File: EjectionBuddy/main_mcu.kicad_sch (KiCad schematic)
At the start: 8 parts, among them SW2 SW_Push, SW3 SW_Push, U11 ESP32-S3-MINI-1

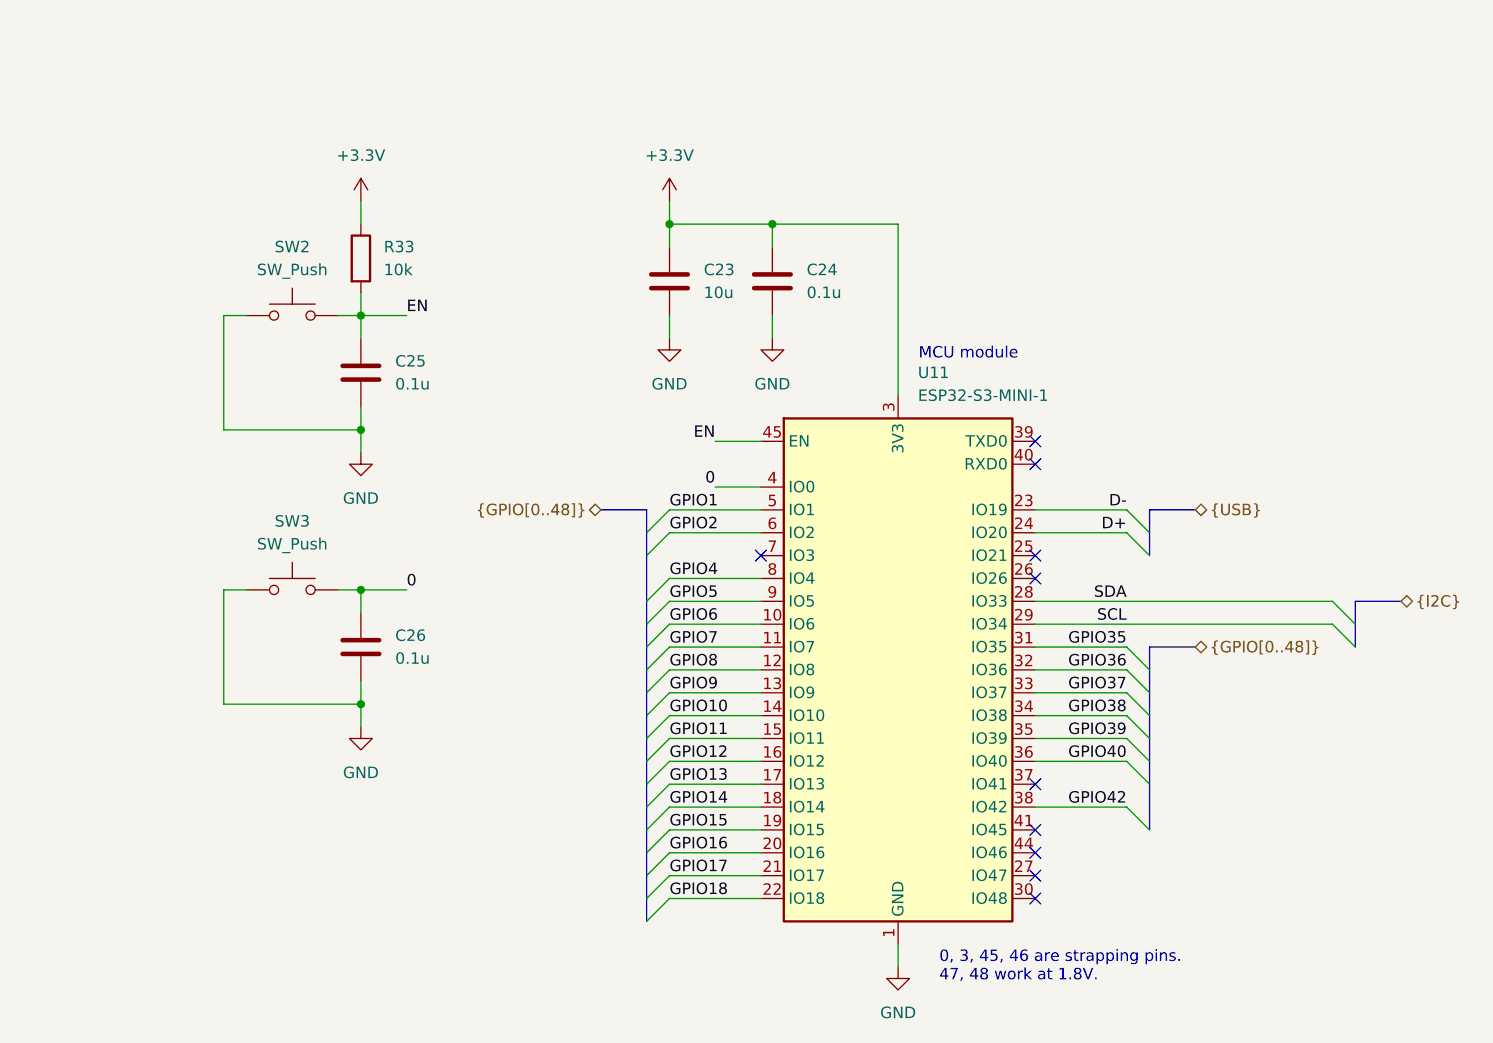
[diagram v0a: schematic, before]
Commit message: Slight improvements on routing and schematic
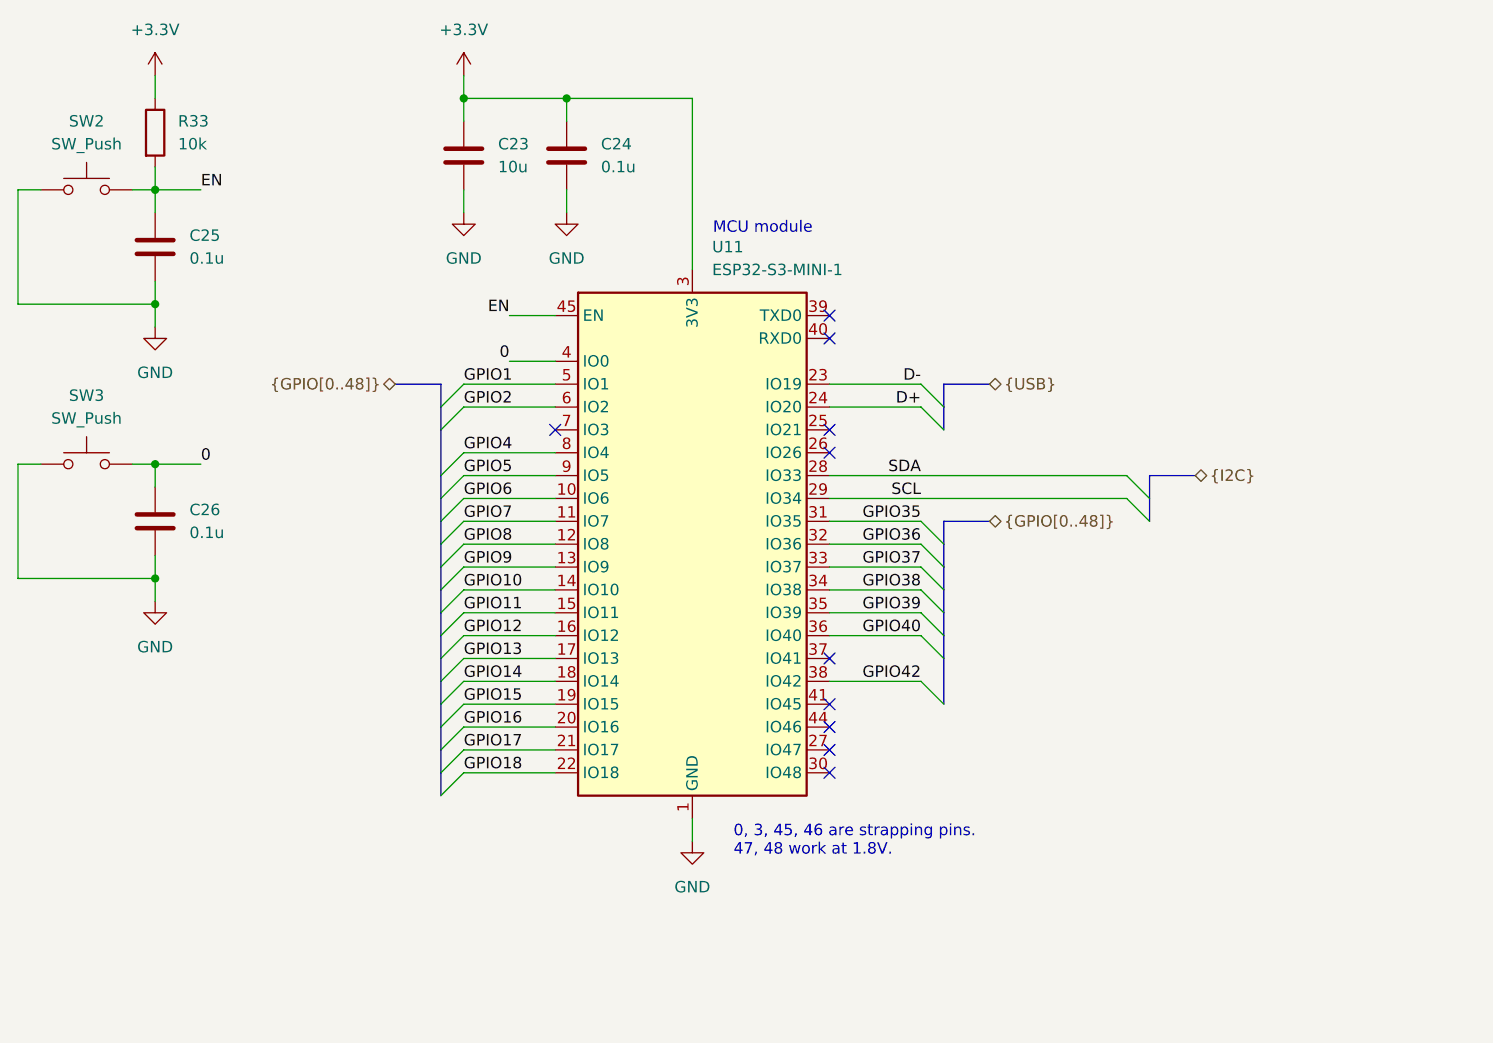
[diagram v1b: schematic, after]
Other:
- moved on the sheet: C23, C24, C25, C26, R33, SW2, SW3, U11

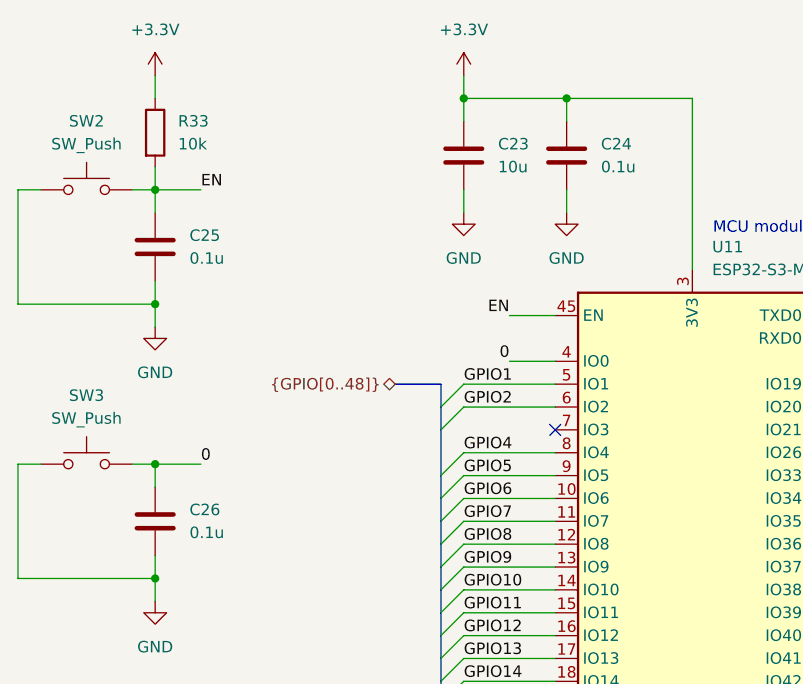
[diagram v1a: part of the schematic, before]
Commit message: Side-mcu stm -> attiny, with improvements here and there
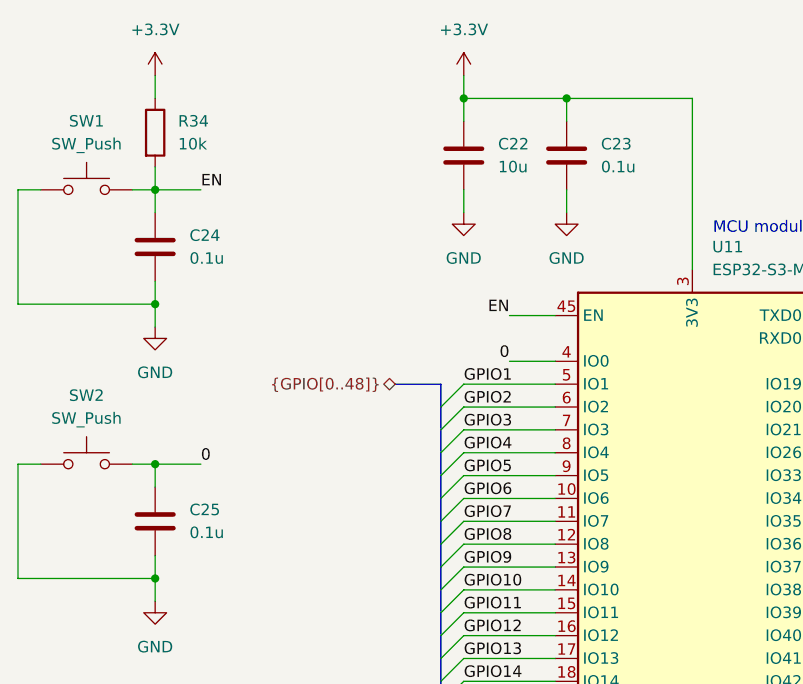
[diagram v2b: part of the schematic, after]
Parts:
- renumbered C23 to C22, C24 to C23, C25 to C24, C26 to C25, R33 to R34, SW2 to SW1, SW3 to SW2
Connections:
- net GPIO3: now reaches U11.7 (IO3)
- no-connect marks 10 -> 9
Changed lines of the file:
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@@
-	)
-	(no_connect
-		(at 85.09 68.58)
 	)
 	(no_connect
@@
 	)
 	(bus_entry
+		(at 72.39 71.12)
+		(size 2.54 -2.54)
+		(stroke
+			(width 0)
+			(type default)
+		)
+	)
+	(bus_entry
 		(at 72.39 83.82)
 		(size 2.54 -2.54)
@@
 	(bus
 		(pts
-			(xy 72.39 68.58) (xy 72.39 73.66)
+			(xy 72.39 68.58) (xy 72.39 71.12)
 		)
 		(stroke
@@
 	(wire
 		(pts
+			(xy 74.93 68.58) (xy 85.09 68.58)
+		)
+		(stroke
+			(width 0)
+			(type default)
+		)
+	)
+	(wire
+		(pts
 			(xy 74.93 73.66) (xy 85.09 73.66)
 		)
@@
 		(pts
 			(xy 40.64 85.09) (xy 40.64 82.55)
+		)
+		(stroke
+			(width 0)
+			(type default)
+		)
+	)
+	(bus
+		(pts
+			(xy 72.39 71.12) (xy 72.39 73.66)
 		)
 		(stroke
@@
 	(label "GPIO10"
 		(at 74.93 86.36 0)
+		(effects
+			(font
+				(size 1.27 1.27)
+			)
+			(justify left bottom)
+		)
+	)
+	(label "GPIO3"
+		(at 74.93 68.58 0)
 		(effects
 			(font
@@
 		(on_board yes)
 		(dnp no)
-		(property "Reference" "#PWR0133"
+		(property "Reference" "#PWR0134"
 			(at 74.93 33.02 0)
 			(effects
@@
 			(project "EjectionBuddy"
 				(path "/8eb0a75f-d01a-4f77-b089-39fac6868a70/f60ca67f-bd6f-453e-97df-667a005ff983"
-					(reference "#PWR0133")
+					(reference "#PWR0134")
 					(unit 1)
 				)
@@
 		(dnp no)
 		(fields_autoplaced yes)
-		(property "Reference" "C23"
+		(property "Reference" "C22"
 			(at 78.74 36.8299 0)
 			(effects
@@
 			(project "EjectionBuddy"
 				(path "/8eb0a75f-d01a-4f77-b089-39fac6868a70/f60ca67f-bd6f-453e-97df-667a005ff983"
-					(reference "C23")
+					(reference "C22")
 					(unit 1)
 				)
@@
 		(dnp no)
 		(fields_autoplaced yes)
-		(property "Reference" "R33"
+		(property "Reference" "R34"
 			(at 43.18 34.2899 0)
 			(effects
@@
 			(project "EjectionBuddy"
 				(path "/8eb0a75f-d01a-4f77-b089-39fac6868a70/f60ca67f-bd6f-453e-97df-667a005ff983"
-					(reference "R33")
+					(reference "R34")
 					(unit 1)
 				)
@@
 		(dnp no)
 		(fields_autoplaced yes)
-		(property "Reference" "#PWR0138"
+		(property "Reference" "#PWR0139"
 			(at 100.33 120.65 0)
 			(effects
@@
 			(project "EjectionBuddy"
 				(path "/8eb0a75f-d01a-4f77-b089-39fac6868a70/f60ca67f-bd6f-453e-97df-667a005ff983"
-					(reference "#PWR0138")
+					(reference "#PWR0139")
 					(unit 1)
 				)
@@
 		(dnp no)
 		(fields_autoplaced yes)
-		(property "Reference" "#PWR0135"
+		(property "Reference" "#PWR0136"
 			(at 86.36 50.8 0)
 			(effects
@@
 			(project "EjectionBuddy"
 				(path "/8eb0a75f-d01a-4f77-b089-39fac6868a70/f60ca67f-bd6f-453e-97df-667a005ff983"
-					(reference "#PWR0135")
+					(reference "#PWR0136")
 					(unit 1)
 				)
@@
 		(dnp no)
 		(fields_autoplaced yes)
-		(property "Reference" "C25"
+		(property "Reference" "C24"
 			(at 44.45 46.9899 0)
 			(effects
@@
 			(project "EjectionBuddy"
 				(path "/8eb0a75f-d01a-4f77-b089-39fac6868a70/f60ca67f-bd6f-453e-97df-667a005ff983"
-					(reference "C25")
+					(reference "C24")
 					(unit 1)
 				)
@@
 		(on_board yes)
 		(dnp no)
-		(property "Reference" "#PWR0132"
+		(property "Reference" "#PWR0133"
 			(at 40.64 33.02 0)
 			(effects
@@
 			(project "EjectionBuddy"
 				(path "/8eb0a75f-d01a-4f77-b089-39fac6868a70/f60ca67f-bd6f-453e-97df-667a005ff983"
-					(reference "#PWR0132")
+					(reference "#PWR0133")
 					(unit 1)
 				)
@@
 		(dnp no)
 		(fields_autoplaced yes)
-		(property "Reference" "SW2"
+		(property "Reference" "SW1"
 			(at 33.02 34.29 0)
 			(effects
@@
 			(project "EjectionBuddy"
 				(path "/8eb0a75f-d01a-4f77-b089-39fac6868a70/f60ca67f-bd6f-453e-97df-667a005ff983"
-					(reference "SW2")
+					(reference "SW1")
 					(unit 1)
 				)
@@
 		(dnp no)
 		(fields_autoplaced yes)
-		(property "Reference" "SW3"
+		(property "Reference" "SW2"
 			(at 33.02 64.77 0)
 			(effects
@@
 			(project "EjectionBuddy"
 				(path "/8eb0a75f-d01a-4f77-b089-39fac6868a70/f60ca67f-bd6f-453e-97df-667a005ff983"
-					(reference "SW3")
+					(reference "SW2")
 					(unit 1)
 				)
@@
 		(dnp no)
 		(fields_autoplaced yes)
-		(property "Reference" "C26"
+		(property "Reference" "C25"
 			(at 44.45 77.4699 0)
 			(effects
@@
 			(project "EjectionBuddy"
 				(path "/8eb0a75f-d01a-4f77-b089-39fac6868a70/f60ca67f-bd6f-453e-97df-667a005ff983"
-					(reference "C26")
+					(reference "C25")
 					(unit 1)
 				)
@@
 		(on_board yes)
 		(dnp no)
-		(property "Reference" "#PWR0137"
+		(property "Reference" "#PWR0138"
 			(at 40.64 93.98 0)
 			(effects
@@
 			(project "EjectionBuddy"
 				(path "/8eb0a75f-d01a-4f77-b089-39fac6868a70/f60ca67f-bd6f-453e-97df-667a005ff983"
-					(reference "#PWR0137")
+					(reference "#PWR0138")
 					(unit 1)
 				)
@@
 		(on_board yes)
 		(dnp no)
-		(property "Reference" "#PWR0134"
+		(property "Reference" "#PWR0135"
 			(at 74.93 50.8 0)
 			(effects
@@
 			(project "EjectionBuddy"
 				(path "/8eb0a75f-d01a-4f77-b089-39fac6868a70/f60ca67f-bd6f-453e-97df-667a005ff983"
-					(reference "#PWR0134")
+					(reference "#PWR0135")
 					(unit 1)
 				)
@@
 		(on_board yes)
 		(dnp no)
-		(property "Reference" "#PWR0136"
+		(property "Reference" "#PWR0137"
 			(at 40.64 63.5 0)
 			(effects
@@
 			(project "EjectionBuddy"
 				(path "/8eb0a75f-d01a-4f77-b089-39fac6868a70/f60ca67f-bd6f-453e-97df-667a005ff983"
-					(reference "#PWR0136")
+					(reference "#PWR0137")
 					(unit 1)
 				)
@@
 		(dnp no)
 		(fields_autoplaced yes)
-		(property "Reference" "C24"
+		(property "Reference" "C23"
 			(at 90.17 36.8299 0)
 			(effects
@@
 			(project "EjectionBuddy"
 				(path "/8eb0a75f-d01a-4f77-b089-39fac6868a70/f60ca67f-bd6f-453e-97df-667a005ff983"
-					(reference "C24")
+					(reference "C23")
 					(unit 1)
 				)

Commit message: Prodection version hw1.0 finished, with tidy-ups and bug-fixes
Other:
- moved on the sheet: C22, C23, C24, C25, R34, SW1, SW2, U11

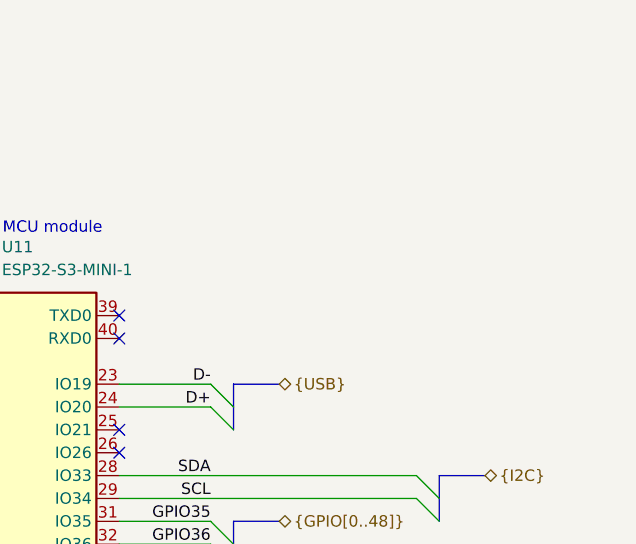
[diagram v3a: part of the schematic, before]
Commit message: Untrack sch renaming poop and renamed connecter.sch to connector.sch
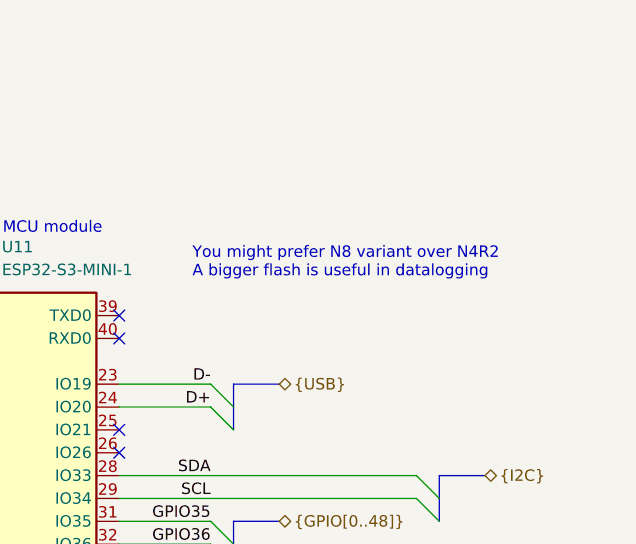
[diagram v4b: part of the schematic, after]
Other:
- note added: "You might prefer N8 variant over N4R2 A bigger flash is useful in datalogging"
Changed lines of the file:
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@@
 	(generator_version "9.0")
 	(paper "A4")
+	(text "You might prefer N8 variant over N4R2\nA bigger flash is useful in datalogging"
+		(exclude_from_sim no)
+		(at 127.508 52.578 0)
+		(effects
+			(font
+				(size 1.27 1.27)
+			)
+			(justify left)
+		)
+	)
 	(text "MCU module"
 		(exclude_from_sim no)
